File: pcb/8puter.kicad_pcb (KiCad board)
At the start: 2 copper layers, 120 x 100 mm, 81 parts, among them J1 PWR-DC, U2 74AHC74, U6 MAX811TEUS+T, X1 ECS-2200BX-100, Y1 1.8432MHz

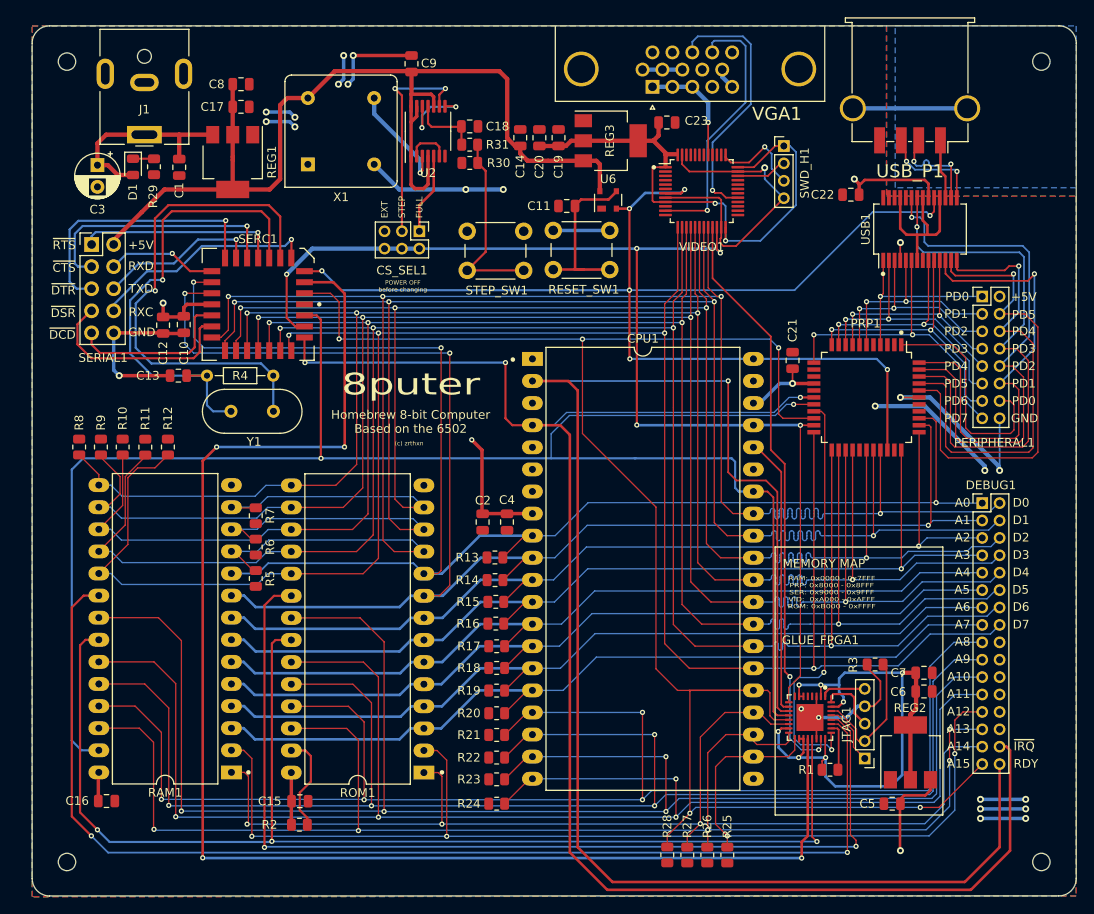
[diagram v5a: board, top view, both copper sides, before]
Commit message: fix peripherals, add SPI
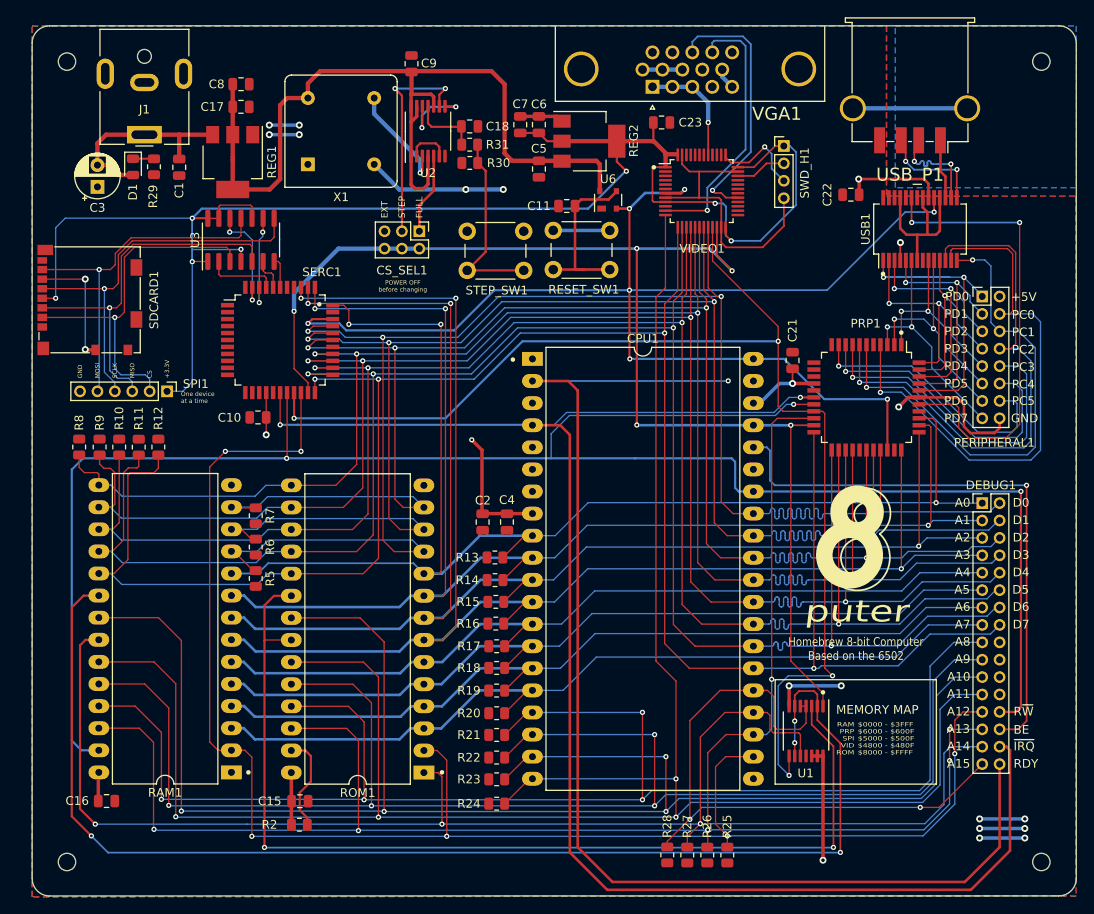
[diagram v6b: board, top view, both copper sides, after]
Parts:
- removed C12, C20: 100nF, Capacitor_SMD:C_0805_2012Metric
- removed C13: 30pF, Capacitor_SMD:C_0805_2012Metric
- removed C14: 10uF, Capacitor_SMD:C_0805_2012Metric
- removed C19: 1uF, Capacitor_SMD:C_0805_2012Metric
- removed GLUE_FPGA1: LCMXO2-256-QFN32, Package_DFN_QFN:QFN-32-1EP_5x5mm_P0.5mm_EP3.1x3.1mm
- removed JTAG1: PIN_HDR, Connector_PinHeader_2.00mm:PinHeader_1x05_P2.00mm_Vertical
- removed R1: 1K, Resistor_SMD:R_0805_2012Metric
- removed R3: 4.7K, Resistor_SMD:R_0805_2012Metric
- removed R4: 1M, Resistor_THT:R_Axial_DIN0204_L3.6mm_D1.6mm_P7.62mm_Horizontal
- removed REG3: NCP1117ST33T3G, Package_TO_SOT_SMD:SOT-223-3_TabPin2
- removed SERIAL1: Conn_02x05_Odd_Even, Connector_PinHeader_2.54mm:PinHeader_2x05_P2.54mm_Vertical
- removed Y1: 1.8432MHz, Crystal:Crystal_HC49-4H_Vertical
- added SDCARD1: Micro_SD_Card, Connector_Card:microSD_HC_Molex_104031-0811, F.Cu at (95.3, 66.7)
- added SPI1: Conn_01x06, Connector_PinHeader_2.00mm:PinHeader_1x06_P2.00mm_Vertical, F.Cu at (104.2, 77.2)
- added U1: 74AC00, Package_SO:TSSOP-14_4.4x5mm_P0.65mm, F.Cu at (177.6, 116.3)
- added U3: 74HC126, Package_SO:SOIC-14_3.9x8.7mm_P1.27mm, F.Cu at (112.7, 59.8)
- R29: value 4K7 -> 1.5K
- SERC1: value W65C51NxPL -> W65C22SxQ; footprint Package_LCC:PLCC-28 -> Package_QFP:PQFP-44_10x10mm_P0.8mm
- VGA1: value DB15_Female -> DB15_Female_HighDensity
- VIDEO1: value STM32F301C6Tx -> STM32F301C8T6; footprint Package_QFP:LQFP-48_7x7mm_P0.5mm -> Package_QFP:TQFP-48_7x7mm_P0.5mm
- moved C5 83.5 mm to (146.9, 51.7), turned to -90 degrees
- moved REG2 79.4 mm to (152.7, 48.5), turned to 0 degrees
- moved C6 78.8 mm to (146.9, 46.6), turned to 90 degrees
- moved C7 78.3 mm to (144.8, 46.6), turned to 90 degrees
- moved C10 13.7 mm to (114.6, 80.2), turned to 0 degrees
- moved SERC1 4.82 mm to (117.2, 71.3), turned to 0 degrees
- moved C3 2.50 mm to (96.2, 53.7), turned to 90 degrees
- moved R12 1.10 mm to (103.2, 83.6)
- moved R11 0.75 mm to (100.9, 83.7)
- moved C23 0.60 mm to (161.0, 46.3)
- moved R10 0.40 mm to (98.7, 83.6)
- moved R9 0.15 mm to (96.4, 83.6)
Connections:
- C23 pad 1: +3V0 -> +3V3
- C3 pad 1: /Power/PWR -> GND
- C3 pad 2: GND -> /Power/PWR
- DEBUG1 pad 26: unconnected-(DEBUG1-Pad26) -> CPU_R~{W}
- DEBUG1 pad 28: unconnected-(DEBUG1-Pad28) -> BE
- PRP1 pad 1: /Peripheral Handler/PC5 -> /Peripheral Handler/PD5
- PRP1 pad 10: /Peripheral Handler/PD5 -> /Peripheral Handler/PC5
- PRP1 pad 11: /Peripheral Handler/PD6 -> unconnected-(PRP1-Pad11)
- PRP1 pad 12: /Peripheral Handler/PD7 -> unconnected-(PRP1-Pad12)
- PRP1 pad 2: Net-(PRP1-Pad2) -> /Peripheral Handler/PD6
- PRP1 pad 20: ADDR15 -> ADDR13
- PRP1 pad 3: Net-(PRP1-Pad3) -> /Peripheral Handler/PD7
- PRP1 pad 38: unconnected-(PRP1-Pad38) -> Net-(PRP1-Pad38)
- PRP1 pad 4: /Peripheral Handler/PD0 -> /Peripheral Handler/PC0
- PRP1 pad 40: /Peripheral Handler/PC0 -> /Peripheral Handler/PD0
- PRP1 pad 41: /Peripheral Handler/PC1 -> /Peripheral Handler/PD1
- PRP1 pad 42: /Peripheral Handler/PC2 -> /Peripheral Handler/PD2
- PRP1 pad 43: /Peripheral Handler/PC3 -> /Peripheral Handler/PD3
- PRP1 pad 44: /Peripheral Handler/PC4 -> /Peripheral Handler/PD4
- PRP1 pad 6: /Peripheral Handler/PD1 -> /Peripheral Handler/PC1
- PRP1 pad 7: /Peripheral Handler/PD2 -> /Peripheral Handler/PC2
- PRP1 pad 8: /Peripheral Handler/PD3 -> /Peripheral Handler/PC3
- PRP1 pad 9: /Peripheral Handler/PD4 -> /Peripheral Handler/PC4
- RAM1 pad 1: ADDR14 -> GND
- RAM1 pad 22: CPU_W~{R} -> ADDR14
- ROM1 pad 22: CPU_W~{R} -> ~{RAM_CS}
- SERC1 pad 1: GND -> unconnected-(SERC1-Pad1)
- SERC1 pad 10: Net-(SERC1-Pad10) -> unconnected-(SERC1-Pad10)
- SERC1 pad 11: Net-(SERIAL1-Pad5) -> unconnected-(SERC1-Pad11)
- SERC1 pad 12: Net-(SERC1-Pad12) -> unconnected-(SERC1-Pad12)
- SERC1 pad 13: ADDR0 -> unconnected-(SERC1-Pad13)
- SERC1 pad 14: ADDR1 -> unconnected-(SERC1-Pad14)
- SERC1 pad 16: Net-(SERIAL1-Pad9) -> unconnected-(SERC1-Pad16)
- SERC1 pad 17: Net-(SERIAL1-Pad7) -> ~{IRQ}
- SERC1 pad 18: DATA0 -> CPU_R~{W}
- SERC1 pad 19: DATA1 -> ~{PRP_CS}
- SERC1 pad 2: ADDR15 -> unconnected-(SERC1-Pad2)
- SERC1 pad 20: DATA2 -> ADDR12
- SERC1 pad 21: DATA3 -> CLOCK
- SERC1 pad 22: DATA4 -> DATA7
- SERC1 pad 23: DATA5 -> DATA6
- SERC1 pad 24: DATA6 -> DATA5
- SERC1 pad 25: DATA7 -> DATA4
- SERC1 pad 26: ~{IRQ} -> DATA3
- SERC1 pad 27: CLOCK -> unconnected-(SERC1-Pad27)
- SERC1 pad 28: CPU_R~{W} -> DATA2
- SERC1 pad 3: ~{SERIAL_CS} -> unconnected-(SERC1-Pad3)
- SERC1 pad 4: ~{RESET} -> unconnected-(SERC1-Pad4)
- SERC1 pad 5: Net-(SERC1-Pad5) -> unconnected-(SERC1-Pad5)
- SERC1 pad 6: Net-(Y1-Pad2) -> unconnected-(SERC1-Pad6)
- SERC1 pad 7: Net-(Y1-Pad1) -> unconnected-(SERC1-Pad7)
- SERC1 pad 8: Net-(SERIAL1-Pad1) -> unconnected-(SERC1-Pad8)
- SERC1 pad 9: Net-(SERIAL1-Pad3) -> unconnected-(SERC1-Pad9)
- SWD_H1 pad 1: +3V0 -> +3V3
- USB1 pad 12: /Peripheral Handler/PC4 -> /Peripheral Handler/PC2
- USB1 pad 22: /Peripheral Handler/PC2 -> unconnected-(USB1-Pad22)
- USB1 pad 23: /Peripheral Handler/PC3 -> Net-(PRP1-Pad38)
- VIDEO1 pad 1: +3V0 -> +3V3
- VIDEO1 pad 12: unconnected-(VIDEO1-Pad12) -> ADDR11
- VIDEO1 pad 21: ~{VID_CS} -> ~{PRP_CS}
- VIDEO1 pad 24: +3V0 -> +3V3
- VIDEO1 pad 36: +3V0 -> +3V3
- VIDEO1 pad 48: +3V0 -> +3V3
- VIDEO1 pad 9: +3V0 -> +3V3
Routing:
- net ~{SERIAL_CS}: track 168.3 -> 0.00 mm, vias 4 -> 0
- net CPU_W~{R}: track 144.9 -> 0.00 mm, vias 3 -> 0
- net ADDR15: track 194.5 -> 73.4 mm, vias 5 -> 2
- net +3V3: track 73.5 -> 193.4 mm
- net ~{PRP_CS}: track 48.2 -> 142.0 mm, vias 2 -> 4
- net ~{VID_CS}: track 67.6 -> 0.00 mm, vias 2 -> 0
- net ADDR11: track 181.7 -> 247.2 mm
- net +3V0: track 63.8 -> 0.00 mm, vias 2 -> 0
- net ADDR3: track 109.4 -> 170.5 mm, vias 1 -> 3
- net Net-(Y1-Pad2): track 57.9 -> 0.00 mm, vias 1 -> 0
- net ADDR2: track 108.5 -> 165.4 mm, vias 1 -> 3
- net Net-(Y1-Pad1): track 53.9 -> 0.00 mm, vias 1 -> 0
- net Net-(PRP1-Pad38): track 0.00 -> 53.6 mm, vias 0 -> 2
- net GND: track 215.8 -> 170.0 mm, vias 24 -> 17
- net ADDR12: track 140.5 -> 186.3 mm, vias 4 -> 6
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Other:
- board text added: "$0000 - $3FFF $6000 - $600F $5000 - $500F $4800 - $480F $8000 - $FFFF"
- board text added: "+3.3V"
- board text added: "8puter Revision 1.0"
- board text added: "BE"
- board text added: "CS"
- board text added: "Design by Alisamar Husain github.com/zrthxn/8puter GPL-3.0 Apr 2022"
- board text added: "MISO"
- board text added: "MOSI"
- board text added: "One device at a time"
- board text added: "PC0"
- board text added: "PC1"
- board text added: "PC2"
- board text added: "PC3"
- board text added: "PC4"
- board text added: "PC5"
- board text added: "RAM PRP SPI VID ROM"
- board text added: "R~{W}"
- board text added: "SCLK"
- board text added: "puter"
- board text removed: "(c) zrthxn"
- board text removed: "8puter"
- board text removed: "8puter Rev 1"
- board text removed: "ADDR BUS"
- board text removed: "By A. Husain. Apr 2022. github.com/zrthxn/8puter GPL-3.0 License"
- board text removed: "DATA BUS"
- board text removed: "RAM: 0x0000 - 0x7FFF PRP: 0x8000 - 0x8FFF SER: 0x9000 - 0x9FFF VID: 0xA000 - 0xAFFF ROM: 0xB000 - 0xFFFF"
- board text removed: "RXC"
- board text removed: "RXD"
- board text removed: "TXD"
- board text removed: "~{CTS}"
- board text removed: "~{DCD}"
- board text removed: "~{DSR}"
- board text removed: "~{DTR}"
- board text removed: "~{RTS}"

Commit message: Cleanup board
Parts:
- R10, R11, R12, R13, R14, R15, R16, R17, R18, R19, R2, R20, R21, R22, R23, R24, R25, R26, R27, R28, R5, R6, R7, R8, R9: value 10K -> 1K
- moved C3 2.51 mm to (96.2, 51.2), turned to -90 degrees
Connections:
- C3 pad 1: GND -> /Power/PWR
- C3 pad 2: /Power/PWR -> GND
- CPU1 pad 6: ~{NMI} -> unconnected-(CPU1-Pad6)
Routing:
- net RDY: track 142.1 -> 119.5 mm, vias 1 -> 0
- net /Peripheral Handler/PD0: track 39.6 -> 32.0 mm
- net GND: track 170.0 -> 166.8 mm
- net +5V: track 168.6 -> 168.1 mm

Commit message: Clearances
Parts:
- removed SWD_H1: Conn_01x04, Connector_PinHeader_2.00mm:PinHeader_1x04_P2.00mm_Vertical
- added ?: , , F.Cu at (107.9, 132.1)
- added ?: , , F.Cu at (201.5, 132.1)
- added ?: , , F.Cu at (201.5, 38.2)
- added ?: , , F.Cu at (144.2, 38.2)
- added C12: 10uF, Capacitor_SMD:C_0805_2012Metric, F.Cu at (172.8, 64.8)
- added C13: 100nF, Capacitor_SMD:C_0805_2012Metric, F.Cu at (175.5, 56.9)
- added C14: 100nF, Capacitor_SMD:C_0805_2012Metric, F.Cu at (175.5, 50.4)
- added PROG1: Conn_01x05, Connector_PinHeader_2.00mm:PinHeader_1x05_P2.00mm_Vertical, F.Cu at (179.2, 52.9)
- added R1: 1K, Resistor_SMD:R_0805_2012Metric, F.Cu at (174.8, 46.3)
- added R3: 1K, Resistor_SMD:R_0805_2012Metric, F.Cu at (170.5, 46.3)
- added R32: 470R, Resistor_SMD:R_0805_2012Metric, F.Cu at (172.8, 46.3)
- added R33: 470R, Resistor_SMD:R_0805_2012Metric, F.Cu at (168.5, 46.3)
- added R34: 470R, Resistor_SMD:R_0805_2012Metric, F.Cu at (166.2, 46.3)
- added R35: 10K, Resistor_SMD:R_0805_2012Metric, F.Cu at (175.5, 53.6)
- added R4: 1K, Resistor_SMD:R_0805_2012Metric, F.Cu at (164.2, 46.3)
- added ROM_WRITE1: Conn_01x03, Connector_PinHeader_2.00mm:PinHeader_1x03_P2.00mm_Vertical, F.Cu at (125.4, 132.3)
- C11: value 10nF -> 100nF
- R29: value 1.5K -> 1K
- RAM1: value AS6C62256-55PCN -> AS6C62256-55SINTR; footprint Package_DIP:DIP-28_W15.24mm_LongPads -> Package_SO:SOIC-28W_7.5x17.9mm_P1.27mm
- ROM1: value AT28C256 -> AT28HC256E-90SU; footprint Package_DIP:DIP-28_W15.24mm_LongPads -> Package_SO:SOIC-28W_7.5x17.9mm_P1.27mm
- VIDEO1: value STM32F301C8T6 -> PIC32MX270F256D; footprint Package_QFP:TQFP-48_7x7mm_P0.5mm -> Package_QFP:TQFP-44_10x10mm_P0.8mm
- moved D1 24.3 mm to (122.8, 60.5), turned to 180 degrees
- moved R29 23.2 mm to (122.8, 62.9), turned to 180 degrees
- moved U3 21.4 mm to (131.5, 70.1)
- moved C3 21.0 mm to (116.4, 56.9), turned to 0 degrees
- moved R8 20.1 mm to (106.8, 99.2)
- moved R12 20.0 mm to (115.8, 99.2)
- moved R10 20.0 mm to (111.3, 99.2)
- moved R9 20.0 mm to (109.0, 99.2)
- moved R11 20.0 mm to (113.5, 99.2)
- moved SDCARD1 16.2 mm to (111.5, 67.5)
- moved C17 13.3 mm to (124.8, 39.0)
- moved C16 12.6 mm to (109.6, 122.3)
- moved C10 11.6 mm to (114.8, 91.8)
- moved SERC1 11.6 mm to (117.4, 82.9)
- moved J1 11.4 mm to (113.0, 47.7)
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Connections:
- D1 pad 2: /Power/PWR -> +5V
- DEBUG1 pad 18: unconnected-(DEBUG1-Pad18) -> GND
- DEBUG1 pad 20: unconnected-(DEBUG1-Pad20) -> +5V
- DEBUG1 pad 24: unconnected-(DEBUG1-Pad24) -> CLOCK
- R2 pad 2: Net-(ROM1-Pad27) -> Net-(R2-Pad2)
- RAM1 pad 20: ~{ROM_CS} -> ~{RAM_CS}
- ROM1 pad 20: ~{RAM_CS} -> ~{ROM_CS}
- ROM1 pad 22: ~{RAM_CS} -> ~{ROM_CS}
- VGA1 pad 1: /Video/COLOR -> /Video/RED
- VGA1 pad 2: /Video/COLOR -> /Video/GREEN
- VGA1 pad 3: /Video/COLOR -> /Video/BLUE
- VGA1 pad 9: unconnected-(VGA1-Pad9) -> GND
- VIDEO1 pad 1: +3V3 -> DATA7
- VIDEO1 pad 11: /Video/VSYNC -> DATA0
- VIDEO1 pad 12: ADDR11 -> Net-(PROG1-Pad5)
- VIDEO1 pad 13: DATA7 -> Net-(PROG1-Pad4)
- VIDEO1 pad 14: DATA6 -> unconnected-(VIDEO1-Pad14)
- VIDEO1 pad 15: DATA5 -> ~{PRP_CS}
- VIDEO1 pad 16: DATA4 -> GND
- VIDEO1 pad 17: DATA3 -> +3V3
- VIDEO1 pad 18: DATA2 -> ~{RESET}
- VIDEO1 pad 19: DATA1 -> /Video/HSYNC
- VIDEO1 pad 2: unconnected-(VIDEO1-Pad2) -> DATA6
- VIDEO1 pad 20: DATA0 -> /Video/VSYNC
- VIDEO1 pad 21: ~{PRP_CS} -> Net-(VIDEO1-Pad21)
- VIDEO1 pad 22: CLOCK -> Net-(VIDEO1-Pad22)
- VIDEO1 pad 23: GND -> Net-(VIDEO1-Pad23)
- VIDEO1 pad 24: +3V3 -> Net-(R33-Pad2)
- VIDEO1 pad 28: unconnected-(VIDEO1-Pad28) -> +3V3
- VIDEO1 pad 29: /Video/HSYNC -> GND
- VIDEO1 pad 3: unconnected-(VIDEO1-Pad3) -> DATA5
- VIDEO1 pad 33: unconnected-(VIDEO1-Pad33) -> Net-(VIDEO1-Pad33)
- VIDEO1 pad 34: Net-(SWD_H1-Pad2) -> unconnected-(VIDEO1-Pad34)
- VIDEO1 pad 35: GND -> unconnected-(VIDEO1-Pad35)
- VIDEO1 pad 36: +3V3 -> unconnected-(VIDEO1-Pad36)
- VIDEO1 pad 37: Net-(SWD_H1-Pad3) -> unconnected-(VIDEO1-Pad37)
- VIDEO1 pad 39: unconnected-(VIDEO1-Pad39) -> GND
- VIDEO1 pad 4: unconnected-(VIDEO1-Pad4) -> DATA4
- VIDEO1 pad 40: unconnected-(VIDEO1-Pad40) -> +3V3
- VIDEO1 pad 41: /Video/COLOR -> Net-(R34-Pad2)
- VIDEO1 pad 43: unconnected-(VIDEO1-Pad43) -> CLOCK
- VIDEO1 pad 44: unconnected-(VIDEO1-Pad44) -> ADDR11
- VIDEO1 pad 5: unconnected-(VIDEO1-Pad5) -> DATA3
- VIDEO1 pad 6: unconnected-(VIDEO1-Pad6) -> GND
- VIDEO1 pad 7: ~{RESET} -> Net-(C12-Pad1)
- VIDEO1 pad 8: GND -> DATA2
- VIDEO1 pad 9: +3V3 -> DATA1
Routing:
- net GND: track 166.8 -> 201.1 mm, vias 17 -> 22
- net ~{ROM_CS}: track 146.9 -> 113.8 mm
- net ~{RESET}: track 148.4 -> 179.6 mm
- net ADDR11: track 247.2 -> 218.5 mm
- net ADDR10: track 191.8 -> 163.2 mm
- net CLOCK: track 145.8 -> 171.9 mm, vias 5 -> 4
- net +3V3: track 193.4 -> 169.6 mm, vias 7 -> 6
- net ADDR9: track 176.1 -> 155.2 mm
- net ADDR8: track 170.6 -> 152.6 mm
- net ADDR14: track 171.1 -> 153.6 mm
- net Net-(SERC1-Pad42): track 11.6 -> 28.6 mm
- net Net-(SERC1-Pad40): track 3.87 -> 20.7 mm
- net ADDR13: track 200.3 -> 184.0 mm
- net ADDR12: track 186.3 -> 171.1 mm
- net DATA7: track 234.9 -> 219.9 mm, vias 4 -> 6
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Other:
- board size 120 x 100 mm -> 100 x 100 mm
- board text added: "+3V3"
- board text added: "3V3"
- board text added: "CLK"
- board text added: "PGC"
- board text added: "PGD"
- board text added: "RO"
- board text added: "Shift jumper to WR to enable ROM rewrite."
- board text added: "WR"
- board text added: "~{CLR}"
- board text removed: "+3.3V"
